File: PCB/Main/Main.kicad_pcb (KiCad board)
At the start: 2 copper layers, 5 parts, among them J1 PICO LEFT, J2 PICO Right, J3 Screw_Terminal_01x02, J4 TB6612FNG_right, J5 TB6612FNG_left

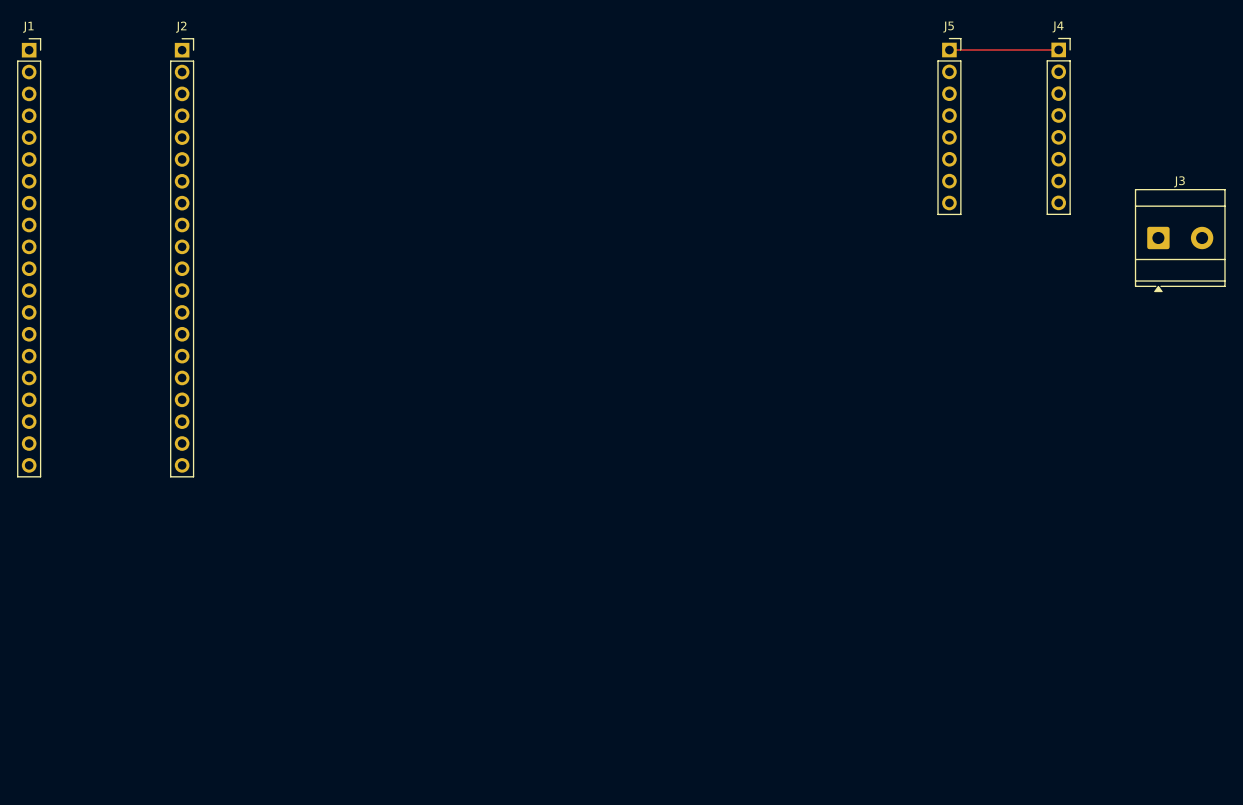
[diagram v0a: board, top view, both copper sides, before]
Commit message: 3step file
Inserted 3step file of nema 17 42x42x23.
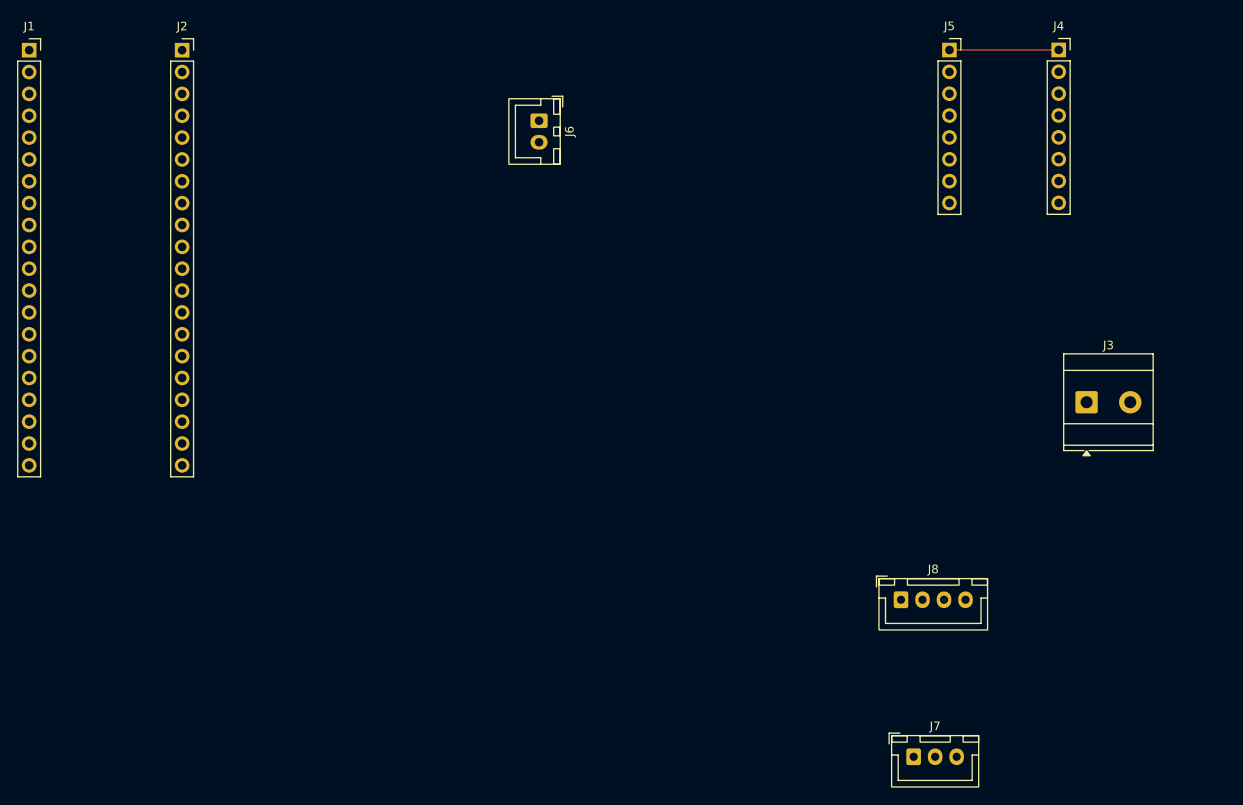
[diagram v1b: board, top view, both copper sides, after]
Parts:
- added J6: Conn_01x02_Socket, Connector_JST:JST_XH_B2B-XH-A_1x02_P2.50mm_Vertical, F.Cu at (159.3, 58.1)
- added J7: Conn_01x03_Socket, Connector_JST:JST_XH_B3B-XH-A_1x03_P2.50mm_Vertical, F.Cu at (202.9, 132.1)
- added J8: Conn_01x04_Socket, Connector_JST:JST_XH_B4B-XH-A_1x04_P2.50mm_Vertical, F.Cu at (201.4, 113.8)
- moved J3 20.8 mm to (223.0, 90.9)
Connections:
- J2 pad 3: unconnected-(J2-Pin_3-Pad3) -> Net-(J2-Pin_3)
- J2 pad 5: unconnected-(J2-Pin_5-Pad5) -> Net-(J2-Pin_5)
